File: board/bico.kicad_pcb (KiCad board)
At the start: 2 copper layers, 21 x 51 mm, 51 parts, among them J1 USB_C_Receptacle_USB2.0, J2 USB_C_Receptacle_USB2.0, J3 Pico_Headers, J4 Conn_01x03, SW1 SW_Push, SW2 SW_Push, SW3 SW_Push, U1 RP2040, U2 W25Q16JV, U3 NCP115ASN330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

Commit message: Start routing
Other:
- copper layers 2 -> 4
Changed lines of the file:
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@@
   (layers
     (0 "F.Cu" signal)
+    (1 "In1.Cu" power)
+    (2 "In2.Cu" power)
     (31 "B.Cu" signal)
     (32 "B.Adhes" user "B.Adhesive")
@@
   )
   (setup
+    (stackup
+      (layer "F.SilkS" (type "Top Silk Screen"))
+      (layer "F.Paste" (type "Top Solder Paste"))
+      (layer "F.Mask" (type "Top Solder Mask") (thickness 0.01))
+      (layer "F.Cu" (type "copper") (thickness 0.035))
+      (layer "dielectric 1" (type "core") (thickness 0.18) (material "FR4") (epsilon_r 4.5) (loss_tangent 0.02))
+      (layer "In1.Cu" (type "copper") (thickness 0.035))
+      (layer "dielectric 2" (type "prepreg") (thickness 1.08) (material "FR4") (epsilon_r 4.5) (loss_tangent 0.02))
+      (layer "In2.Cu" (type "copper") (thickness 0.035))
+      (layer "dielectric 3" (type "core") (thickness 0.18) (material "FR4") (epsilon_r 4.5) (loss_tangent 0.02))
+      (layer "B.Cu" (type "copper") (thickness 0.035))
+      (layer "B.Mask" (type "Bottom Solder Mask") (thickness 0.01))
+      (layer "B.Paste" (type "Bottom Solder Paste"))
+      (layer "B.SilkS" (type "Bottom Silk Screen"))
+      (copper_finish "None")
+      (dielectric_constraints no)
+    )
     (pad_to_mask_clearance 0)
     (pcbplotparams

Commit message: Fully routed
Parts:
- J4: footprint Connector_PinHeader_1.27mm:PinHeader_1x03_P1.27mm_Vertical -> Connector_PinHeader_1.00mm:PinHeader_1x03_P1.00mm_Vertical
- moved R3 13.4 mm to (143.5, 82.0), turned to 180 degrees
- moved R12 12.9 mm to (143.6, 117.8), turned to 180 degrees
- moved D4 12.8 mm to (143.8, 116.2), turned to 0 degrees
- moved R1 12.6 mm to (143.5, 81.0), turned to 180 degrees
- moved R10 11.7 mm to (156.5, 117.5), turned to 0 degrees
- moved D1 6.01 mm to (156.8, 77.5)
- moved C10 4.00 mm to (156.2, 83.0)
- moved C11 4.00 mm to (156.2, 89.0)
- moved U3 4.00 mm to (155.8, 86.0)
- moved J4 2.95 mm to (146.7, 104.5), turned to -90 degrees
- moved R2 2.02 mm to (151.2, 91.8)
- moved R4 2.02 mm to (150.2, 91.8)
- moved C5 1.99 mm to (145.8, 89.5)
- moved U2 1.99 mm to (145.8, 91.3)
- moved R5 1.80 mm to (145.6, 87.5)
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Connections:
- D4 pad 1: Net-(D4-Pad1) -> GND
- D4 pad 2: /P_LED -> Net-(R12-Pad2)
- R12 pad 1: Net-(D4-Pad1) -> /P_LED
- R12 pad 2: GND -> Net-(R12-Pad2)
- SW1 pad 1: GND -> /M_~{RST}
- SW1 pad 2: /M_~{RST} -> GND
- SW2 pad 1: Net-(R5-Pad2) -> GND
- SW2 pad 2: GND -> Net-(R5-Pad2)
- U4 pad 9: /P_LED -> unconnected-(U4-Pad9)
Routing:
- net VSYS: track 0.00 -> 52.3 mm, vias 0 -> 2
- net /GPIO15: track 0.00 -> 29.3 mm
- net /GPIO16: track 0.00 -> 27.9 mm
- net /GPIO14: track 0.00 -> 26.5 mm
- net +3V3: track 0.00 -> 25.7 mm, vias 0 -> 19
- net /GPIO17: track 0.00 -> 24.8 mm
- net /M_~{RST}: track 0.00 -> 23.6 mm, vias 0 -> 3
- net /PROBE_AUX: track 0.00 -> 23.6 mm, vias 0 -> 2
- net /GPIO0: track 0.00 -> 22.6 mm
- net /GPIO13: track 0.00 -> 21.5 mm
- net GND: track 0.00 -> 21.2 mm, vias 0 -> 50
- net /LED: track 0.00 -> 20.9 mm, vias 0 -> 2
- net /UART_M2P: track 0.00 -> 20.7 mm, vias 0 -> 2
- net /GPIO1: track 0.00 -> 20.4 mm
- net /UART_P2M: track 0.00 -> 19.5 mm, vias 0 -> 2
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- added copper zone on F.Cu, net +3V3
- added copper zone on In2.Cu, net +3V3
- added copper zone on F.Cu, net DVDD_M
- added copper zone on F.Cu, net DVDD_P
- added copper zone on B.Cu, net GND
- added copper zone on F.Cu, net GND
- added copper zone on In1.Cu, net GND
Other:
- board text added: "BOOT"
- board text added: "RST"
- board text removed: "Bico"

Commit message: DRC clean, for now
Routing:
- net unconnected-(U4-Pad9): track 1.34 -> 0.00 mm
- net GND: track 21.2 -> 20.5 mm
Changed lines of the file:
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@@
   (via (at 149.6 112.7) (size 0.45) (drill 0.3) (layers "F.Cu" "B.Cu") (free) (net 1))
   (via (at 152.5 112.5) (size 0.45) (drill 0.3) (layers "F.Cu" "B.Cu") (free) (net 1))
-  (via (at 149.975 99.675) (size 0.45) (drill 0.3) (layers "F.Cu" "B.Cu") (free) (net 1))
+  (via (at 150 99.63) (size 0.45) (drill 0.3) (layers "F.Cu" "B.Cu") (free) (net 1))
   (via (at 152.65 94.35) (size 0.45) (drill 0.3) (layers "F.Cu" "B.Cu") (free) (net 1))
   (via (at 154.675 93.775) (size 0.45) (drill 0.3) (layers "F.Cu" "B.Cu") (free) (net 1))
@@
   (segment (start 152.225731 117.425) (end 153.25 116.400731) (width 0.2) (layer "F.Cu") (net 2))
   (segment (start 153.25 116.400731) (end 153.25 115.8) (width 0.2) (layer "F.Cu") (net 2))
-  (segment (start 142.675 114.825) (end 142.675 114.075) (width 0.1) (layer "F.Cu") (net 2))
   (segment (start 150.8 97.8) (end 151.2 98.2) (width 0.2) (layer "F.Cu") (net 2))
   (segment (start 146.78 81.7) (end 146.8 81.68) (width 0.3) (layer "F.Cu") (net 2))
@@
   (via (at 149.25 90.6) (size 0.45) (drill 0.3) (layers "F.Cu" "B.Cu") (free) (net 2))
   (via (at 156.66 85.9) (size 0.45) (drill 0.3) (layers "F.Cu" "B.Cu") (free) (net 2))
-  (via (at 149.1 82.9) (size 0.45) (drill 0.3) (layers "F.Cu" "B.Cu") (free) (net 2))
+  (via (at 149.02 82.93) (size 0.45) (drill 0.3) (layers "F.Cu" "B.Cu") (free) (net 2))
   (via (at 150.8 96.2) (size 0.45) (drill 0.3) (layers "F.Cu" "B.Cu") (free) (net 2))
   (via (at 150.9 82.9) (size 0.45) (drill 0.3) (layers "F.Cu" "B.Cu") (free) (net 2))
@@
   (segment (start 156.85312 95.597498) (end 157.143848 95.597498) (width 0.1) (layer "F.Cu") (net 52))
   (segment (start 148.4 103) (end 148.7 103.3) (width 0.1) (layer "F.Cu") (net 55))
-  (segment (start 148.66 106.44) (end 148.6 106.5) (width 0.1) (layer "F.Cu") (net 55))
   (segment (start 147.25 103) (end 148.4 103) (width 0.1) (layer "F.Cu") (net 55))
   (segment (start 148.7 105.6) (end 148.6 105.7) (width 0.1) (layer "F.Cu") (net 55))
@@
   (segment (start 148.07 92.02) (end 148.390998 92.340998) (width 0.1) (layer "F.Cu") (net 74))
   (segment (start 147.263248 92.02) (end 148.07 92.02) (width 0.1) (layer "F.Cu") (net 74))
-  (segment (start 148.6 93.1) (end 148.6 93.5) (width 0.1) (layer "F.Cu") (net 74))
   (segment (start 144.263248 91.52) (end 144.087728 91.52) (width 0.1) (layer "F.Cu") (net 75))
   (segment (start 144.087728 91.52) (end 143.738248 91.86948) (width 0.1) (layer "F.Cu") (net 75))
   (segment (start 143.738248 91.86948) (end 143.738248 92.17052) (width 0.1) (layer "F.Cu") (net 75))
   (segment (start 148.2 92.825) (end 148.2 93.5) (width 0.1) (layer "F.Cu") (net 75))
-  (segment (start 148.2 93.1) (end 148.2 93.5) (width 0.1) (layer "F.Cu") (net 75))
   (segment (start 143.738248 92.17052) (end 143.968728 92.400998) (width 0.1) (layer "F.Cu") (net 75))
   (segment (start 147.775998 92.400998) (end 148.2 92.825) (width 0.1) (layer "F.Cu") (net 75))
@@
   (segment (start 143.538747 91.568981) (end 143.538747 92.253157) (width 0.1) (layer "F.Cu") (net 76))
   (segment (start 143.538747 92.253157) (end 143.886092 92.600499) (width 0.1) (layer "F.Cu") (net 76))
-  (segment (start 147.8 93.1) (end 147.8 93.5) (width 0.1) (layer "F.Cu") (net 76))
   (segment (start 144.263248 91.02) (end 144.087728 91.02) (width 0.1) (layer "F.Cu") (net 76))
   (segment (start 147.550499 92.600499) (end 147.8 92.85) (width 0.1) (layer "F.Cu") (net 76))
@@
   (segment (start 155.65 115.95) (end 155.4 115.95) (width 0.1) (layer "F.Cu") (net 103))
   (segment (start 155.767363 114.349501) (end 156.124501 114.706639) (width 0.1) (layer "F.Cu") (net 103))
-  (segment (start 153.5 109.4) (end 154.84 109.4) (width 0.1) (layer "F.Cu") (net 104))
   (zone locked (net 2) (net_name "GND") (layers "F.Cu" "In1.Cu" "B.Cu") (hatch edge 0.508)
     (connect_pads (clearance 0.12))

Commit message: Tidy up grounding etc
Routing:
- net /M_~{RST}: track 23.6 -> 24.9 mm
- net Net-(R10-Pad2): track 17.7 -> 16.5 mm
- net /PROBE_AUX: track 23.6 -> 22.9 mm
- net /GPIO1: track 20.4 -> 21.0 mm
- net /GPIO0: track 22.6 -> 23.2 mm
- net /GPIO17: track 24.8 -> 25.4 mm
- net +3V3: track 25.7 -> 25.6 mm, vias 19 -> 23
- net GND: track 20.5 -> 20.4 mm, vias 50 -> 68
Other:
- board text added: "Bico"

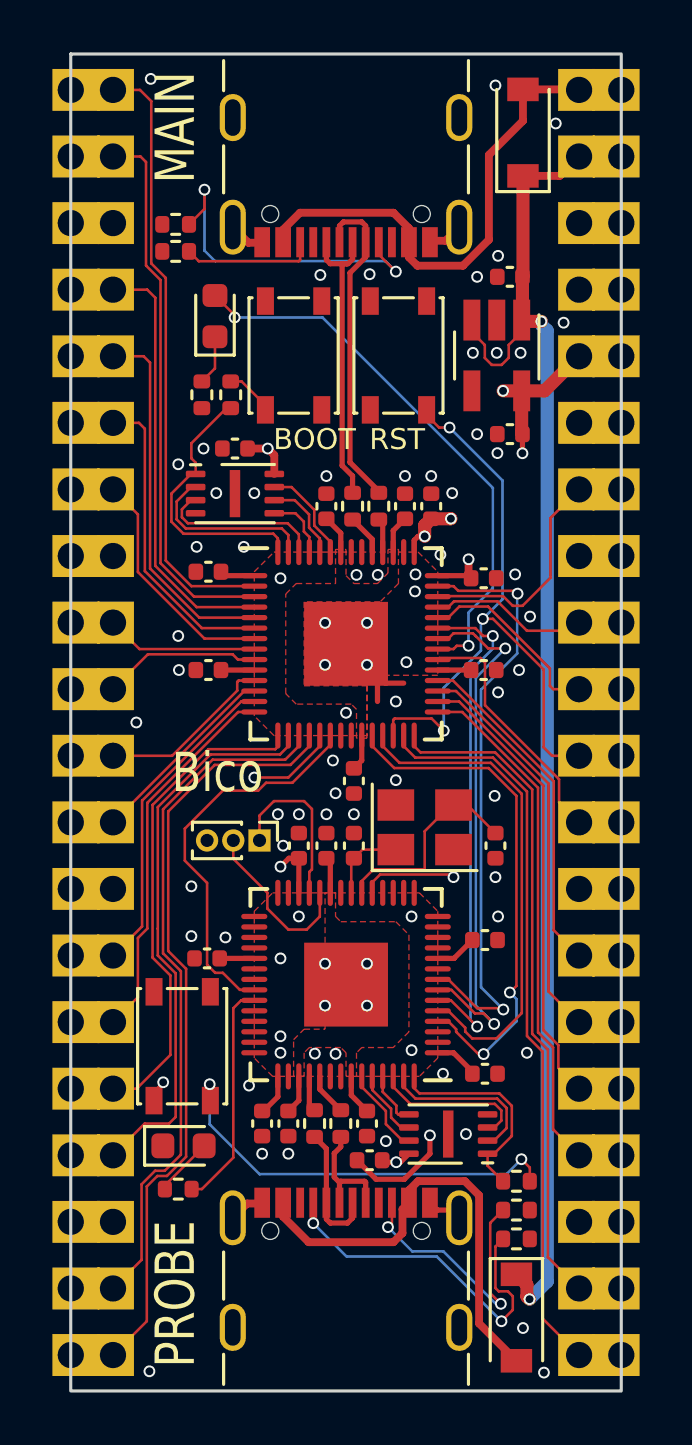
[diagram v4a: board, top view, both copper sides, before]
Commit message: Label all pins in silkscreen
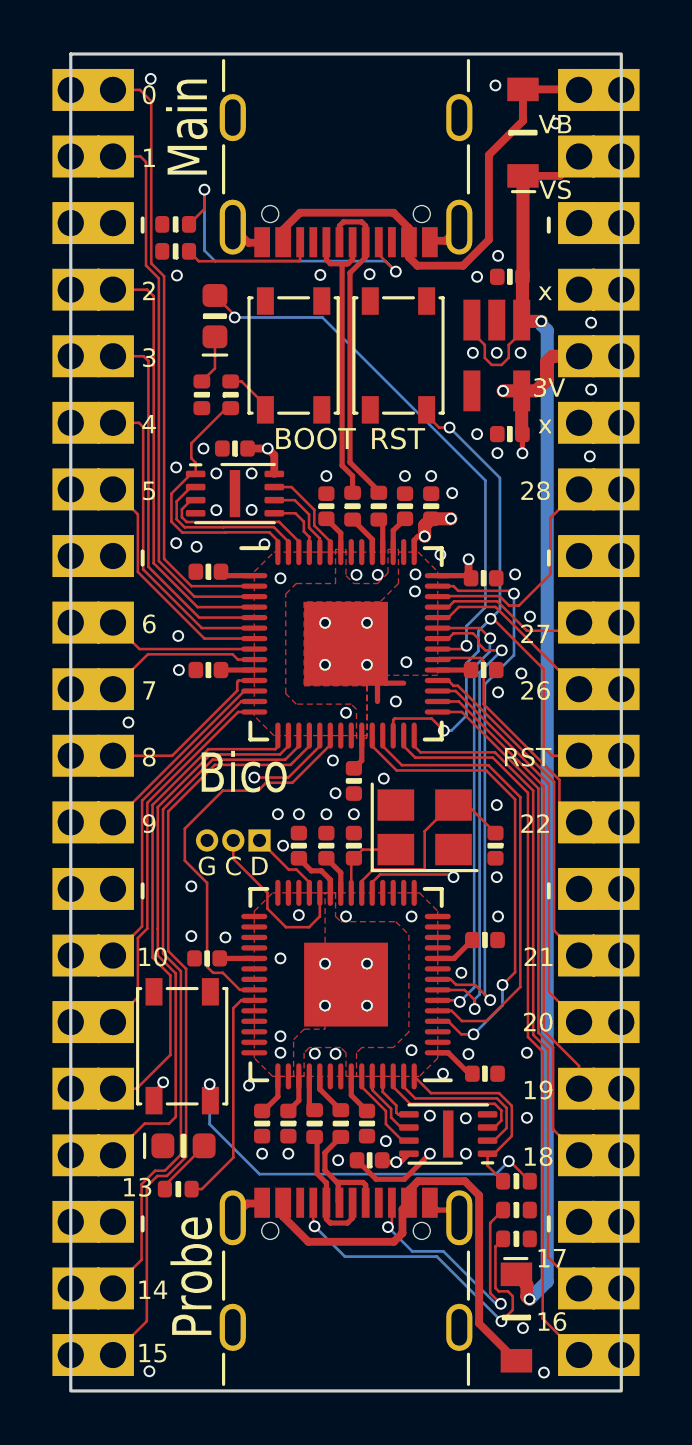
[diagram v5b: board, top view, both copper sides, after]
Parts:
- C1, C10, C11, C12, C13, C14, C15, C16, C17, C18, C19, C2, C20, C21, C22, C3, C4, C5, C6, C7, C8, C9: footprint Capacitor_SMD:C_0402_1005Metric -> bico:C_0402_1005Metric
- D1, D2: footprint Diode_SMD:D_SOD-123 -> bico:D_SOD-123
- D3, D4: footprint LED_SMD:LED_0603_1608Metric -> bico:LED_0603_1608Metric
- J4: footprint Connector_PinHeader_1.00mm:PinHeader_1x03_P1.00mm_Vertical -> bico:PinHeader_1x03_P1.00mm_Vertical
- R1, R10, R11, R12, R2, R3, R4, R5, R6, R7, R8, R9: footprint Resistor_SMD:R_0402_1005Metric -> bico:R_0402_1005Metric
- U3: footprint Package_TO_SOT_SMD:SOT-23-5_HandSoldering -> bico:SOT-23-5_HandSoldering
- moved C15 1.05 mm to (148.2, 104.7)
- moved C19 1.05 mm to (149.2, 104.7)
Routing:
- net /P_SWDIO: track 6.54 -> 2.96 mm
- net /UART_P2M: track 19.5 -> 17.4 mm
- net /UART_M2P: track 20.7 -> 18.9 mm
- net /M_SWCLK: track 19.6 -> 17.9 mm
- net /PROBE_AUX: track 22.9 -> 21.4 mm
- net /M_SWDIO: track 18.9 -> 17.5 mm
- net GND: track 20.4 -> 19.7 mm, vias 68 -> 80
- net DVDD_P: track 4.44 -> 5.09 mm
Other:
- rule pad_to_mask_clearance: 0 -> 0.05
- board text added: "0"
- board text added: "1"
- board text added: "10"
- board text added: "13"
- board text added: "14"
- board text added: "15"
- board text added: "16"
- board text added: "17"
- board text added: "18"
- board text added: "19"
- board text added: "2"
- board text added: "20"
- board text added: "21"
- board text added: "22"
- board text added: "26"
- board text added: "27"
- board text added: "28"
- board text added: "3"
- board text added: "3V"
- board text added: "3V3"
- board text added: "4"
- board text added: "5"
- board text added: "6"
- board text added: "7"
- board text added: "8"
- board text added: "9"
- board text added: "C"
- board text added: "D"
- board text added: "G"
- board text added: "G0"
- board text added: "G1"
- board text added: "G10"
- board text added: "G11"
- board text added: "G12"
- board text added: "G13"
- board text added: "G14"
- board text added: "G15"
- board text added: "G16"
- board text added: "G17"
- board text added: "G18"
- board text added: "G19"
- board text added: "G2"
- board text added: "G20"
- board text added: "G21"
- board text added: "G22"
- board text added: "G26"
- board text added: "G27"
- board text added: "G28"
- board text added: "G3"
- board text added: "G4"
- board text added: "G5"
- board text added: "G6"
- board text added: "G7"
- board text added: "G8"
- board text added: "G9"
- board text added: "GND"
- board text added: "Main"
- board text added: "Probe"
- board text added: "VB"
- board text added: "VBU"
- board text added: "VS"
- board text added: "VSY"
- board text added: "x"
- board text added: "~{RST}"
- board text removed: "MAIN"
- board text removed: "PROBE"

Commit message: Add github link and silk text to board underside
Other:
- board text added: "REV A0"
- board text added: "github.com/ wren6991/bico"
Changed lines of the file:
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@@
     (effects (font (size 1 1) (thickness 0.15)) (justify left mirror))
+  )
+  (gr_text "github.com/\nwren6991/bico" (at 149.987 78.74) (layer "B.SilkS")
+    (effects (font (size 0.8 0.8) (thickness 0.1)) (justify mirror))
   )
   (gr_text "G7" (at 142.0876 98.7552) (layer "B.SilkS")
@@
     (effects (font (size 1 1) (thickness 0.15)) (justify left mirror))
   )
+  (gr_text "REV A0" (at 149.987 121.031) (layer "B.SilkS")
+    (effects (font (size 0.8 0.8) (thickness 0.1)) (justify mirror))
+  )
   (gr_text "G3" (at 142.0876 86.0044) (layer "B.SilkS")

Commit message: Add JLC silk text
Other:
- board text added: "JLCJLCJLCJLC"
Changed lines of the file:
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@@
     (effects (font (size 1 1) (thickness 0.15)) (justify left mirror))
+  )
+  (gr_text "JLCJLCJLCJLC" (at 149.987 87.376) (layer "B.SilkS")
+    (effects (font (size 0.9 0.9) (thickness 0.12)) (justify mirror))
   )
   (gr_text "GND" (at 142.0876 80.9752) (layer "B.SilkS")
